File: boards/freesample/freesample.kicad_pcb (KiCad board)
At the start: 8 copper layers, 124 x 190 mm, 576 parts, among them J1 SMA, J10 XILINX_JTAG, J11 SMA, J12 SMA, J13 SMA, J14 SMA, J15 SMA, J16 SMA, J17 SMA, J18 SMA, J19 JUMPER, J2 BARREL, J20 JUMPER, J21 JUMPER, J22 SMA, J23 SMA, J24 SMA, J25 SMA, J26 PMOD_HOST, J3 SMA, J4 SMA, J5 SMA, J6 XILINX_JTAG, J7 CONN_INTEGRALSTICK_FPGA_HOST, J8 CONN_INTEGRALSTICK_MCU_HOST, J9 0826-1G1T-23-F, M1 TRACEPAD, M2 LOGO1, M3 LOGO2, M4 LOGO3, M5 LOGO4, M6 LOGO5, M7 LOGO6, Q1 SSM6N58NU, U1 HMC675LP3E, U10 PI6C59S6005, U11 PI6C59S6005, U12 PI6C59S6005, U13 SIP32408, U14 LMK04806, U15 ASG-D-V-A-125.000MHZ, U16 HMC856, U17 NB6L295, U18 PI6C59S6005, U19 NB7V52MMNG, U2 HMC675LP3E, U20 NB7V52MMNG, U21 NB7V52MMNG, U22 PI6C59S6005, U26 MCP1755ST-5002E/MC, U27 LM27761, U28 ADP1763Z-1.0, U29 ADP1763Z-1.0, U3 PI6C59S6005, U30 OKL-T/3-W12P-C, U31 ADP1741, U32 OKL-T/3-W12P-C, U33 ADP1741, U34 ADP1741, U35 OKL-T/3-W12P-C, U36 OKL-T/3-W12P-C, U37 LM27761, U38 OKL-T/3-W12P-C, U39 LM27761, U4 LTC2664CUH-16#PBF, U40 DS25BR150, U41 DS25BR150, U42 ADP1741, U43 ADP1741, U5 TLK10232, U6 LMK61PD0A2, U7 PI6C59S6005, U8 HMC675LP3E, U9 HMC675LP3E

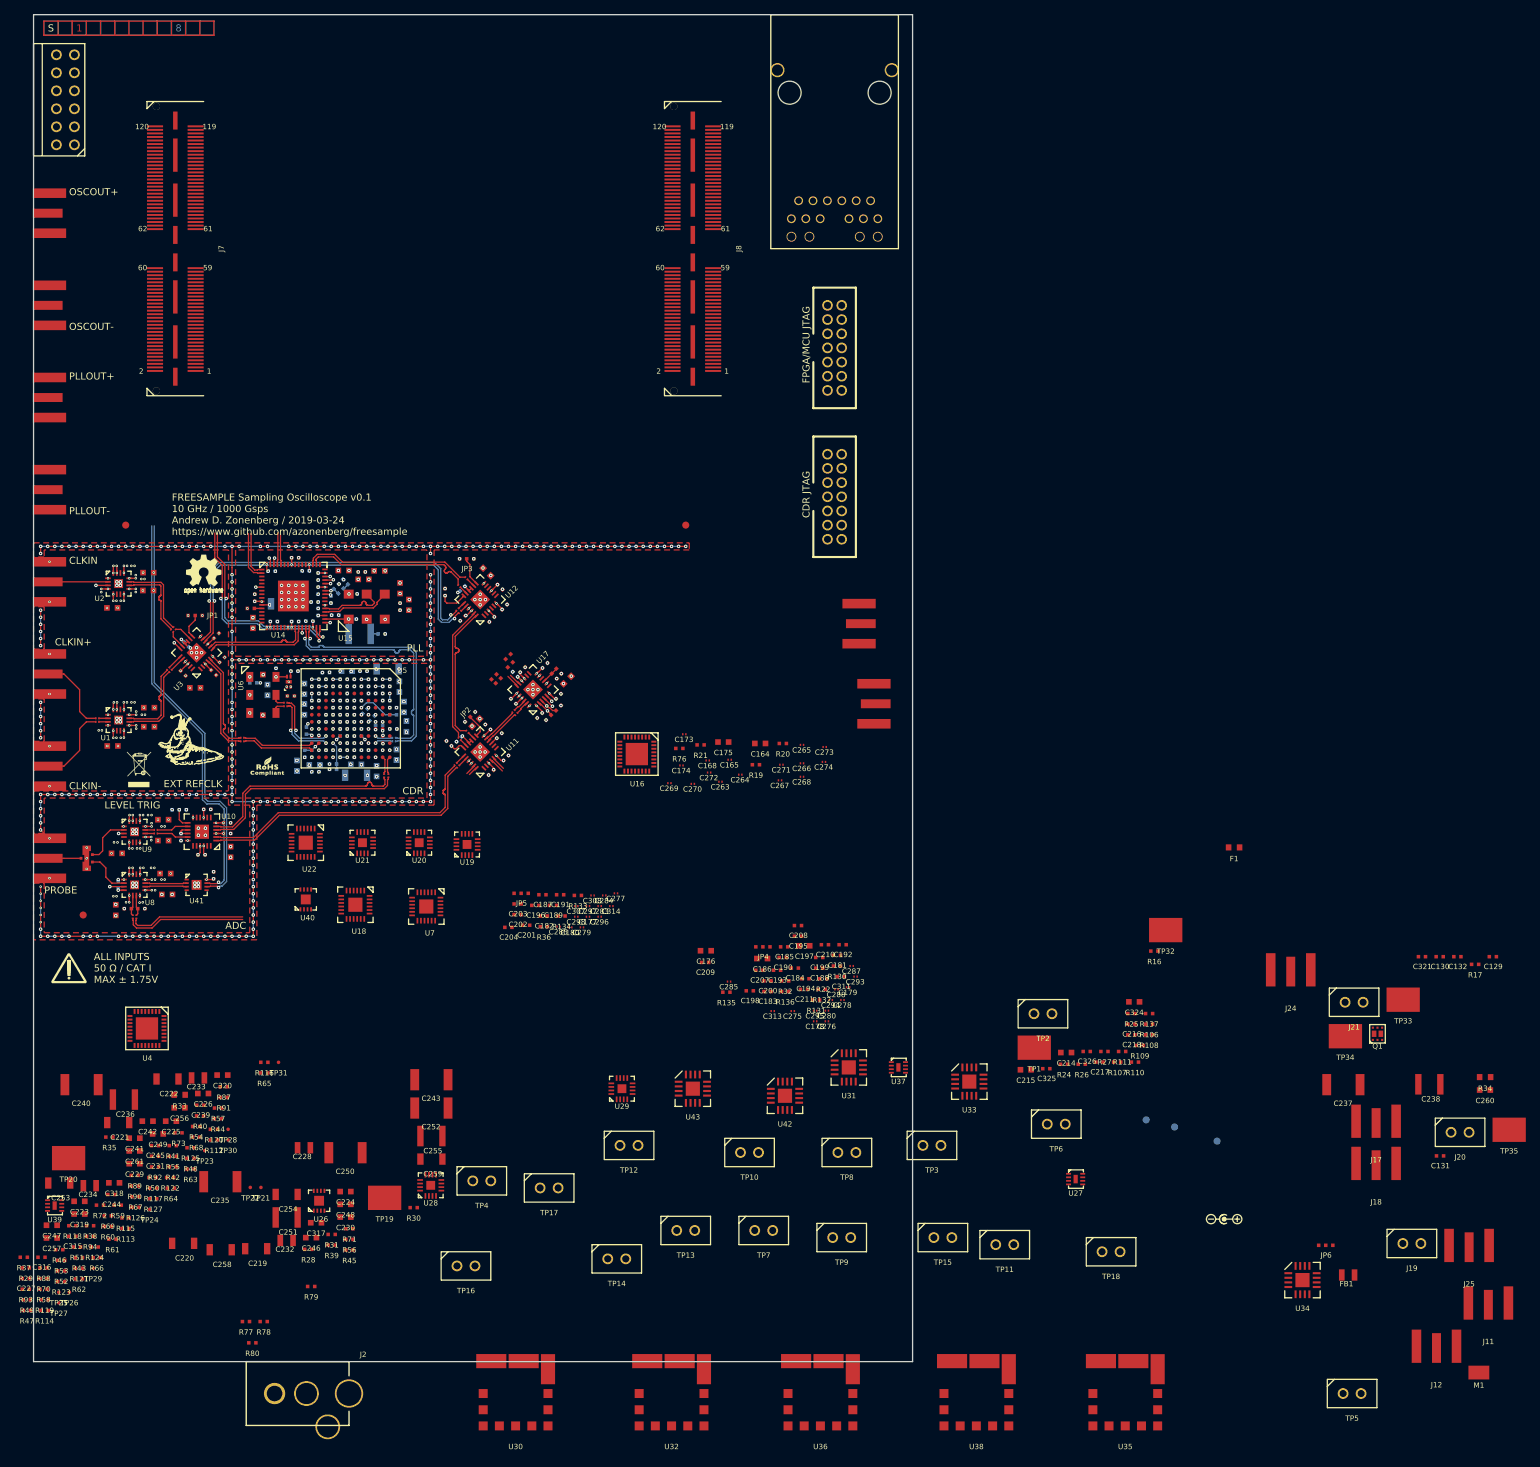
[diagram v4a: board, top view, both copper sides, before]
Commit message: Rearranged a bunch of pending stuff in preparation for further layout. Moved SMAs to approximate final locations
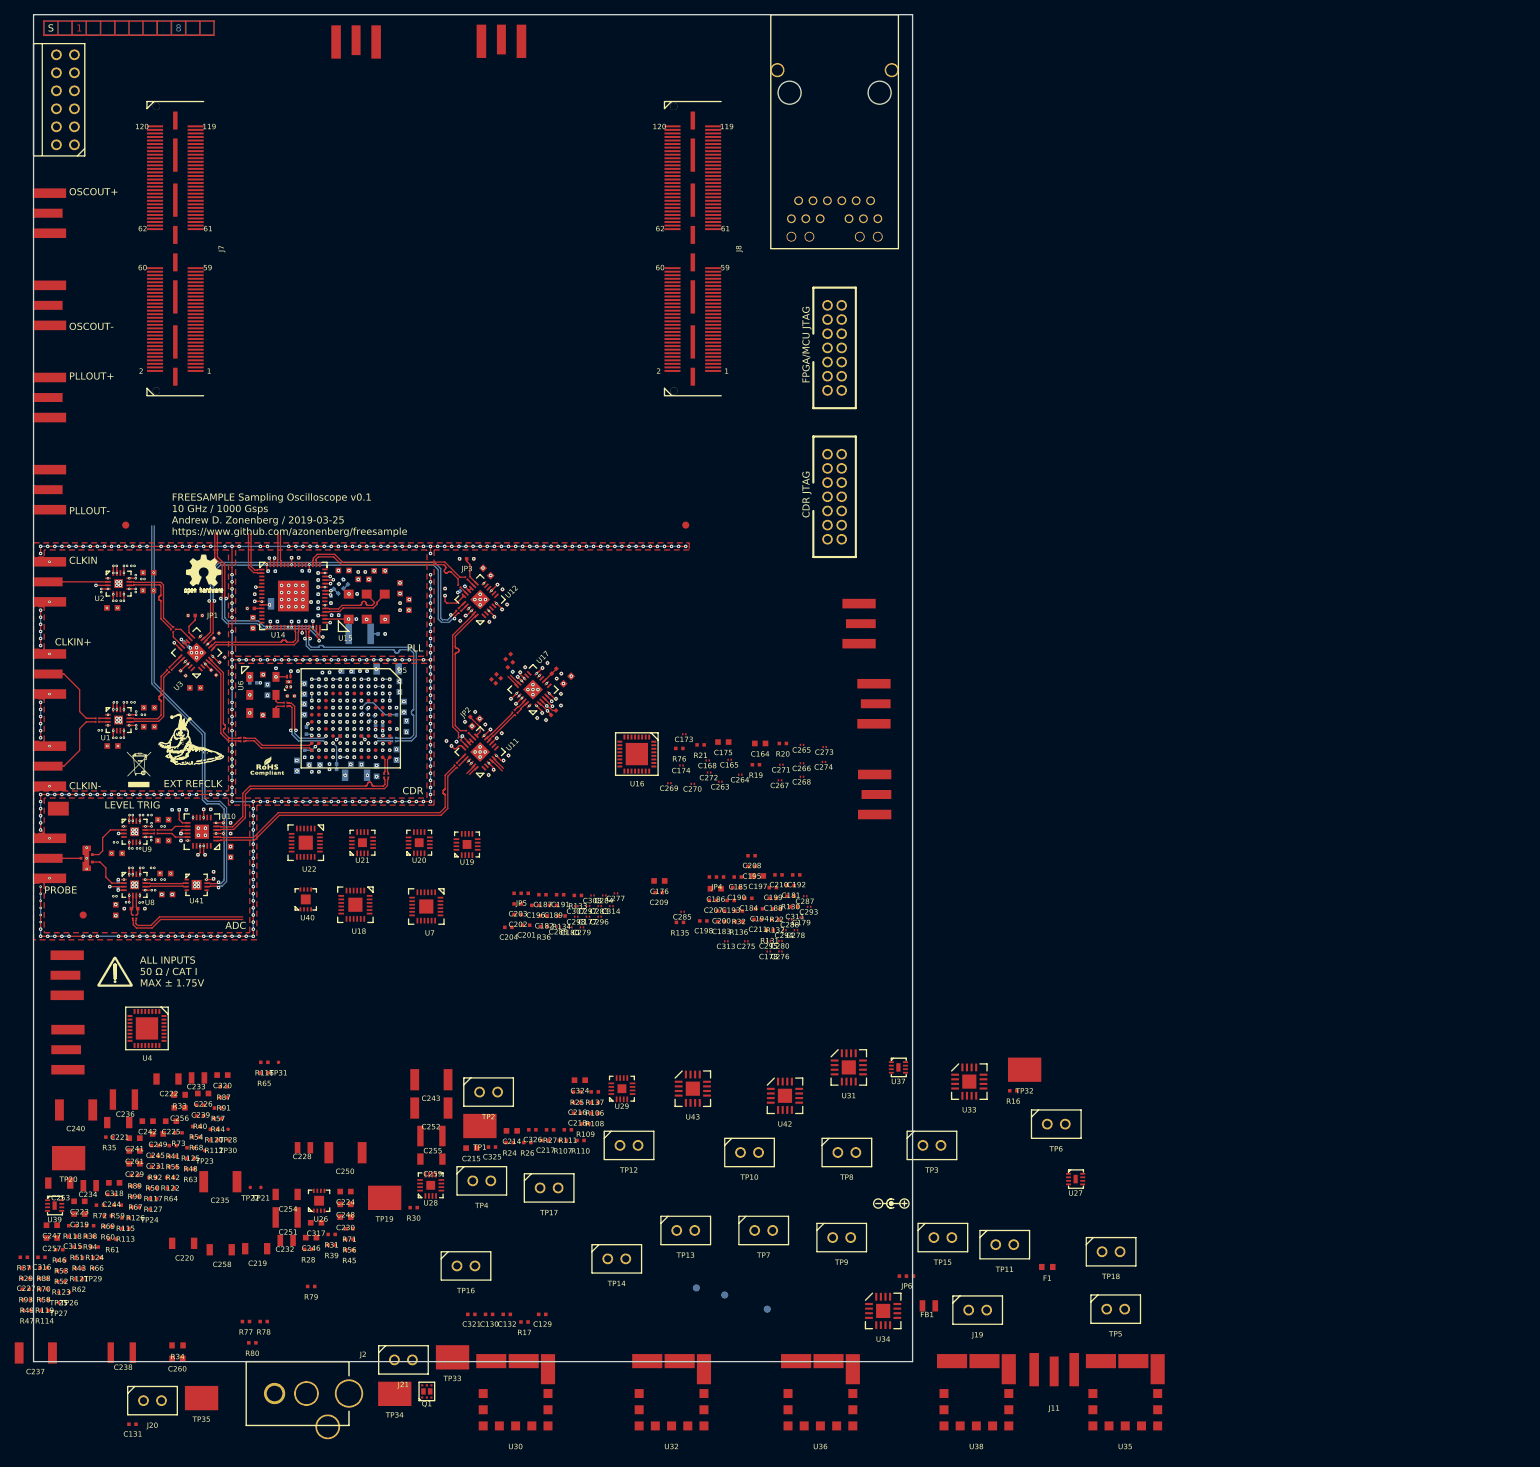
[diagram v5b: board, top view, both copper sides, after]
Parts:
- moved J25 234.7 mm to (61.5, 46.5), turned to 180 degrees
- moved M1 215.6 mm to (19.5, 157.0)
- moved J18 189.2 mm to (18.4, 180.5), turned to 270 degrees
- moved C237 188.3 mm to (16.3, 233.8)
- moved C238 188.3 mm to (28.4, 233.7)
- moved C131 188.3 mm to (30.0, 243.8)
- moved C260 188.3 mm to (36.3, 234.5)
- moved J20 188.3 mm to (32.8, 240.5)
- moved R34 188.3 mm to (36.3, 232.7)
- moved TP35 188.3 mm to (39.7, 240.1)
- moved J17 187.3 mm to (18.5, 191.0), turned to 270 degrees
- moved J24 175.5 mm to (82.0, 46.4), turned to 180 degrees
- moved C129 143.3 mm to (87.8, 228.3)
- moved C130 143.3 mm to (80.3, 228.3)
- moved C132 143.3 mm to (82.8, 228.3)
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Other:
- board text added: "FREESAMPLE Sampling Oscilloscope v0.1 10 GHz / 1000 Gsps Andrew D. Zonenberg / 2019-03-25 https://www.github.com/azonenberg/freesample"
- board text removed: "FREESAMPLE Sampling Oscilloscope v0.1 10 GHz / 1000 Gsps Andrew D. Zonenberg / 2019-03-24 https://www.github.com/azonenberg/freesample"

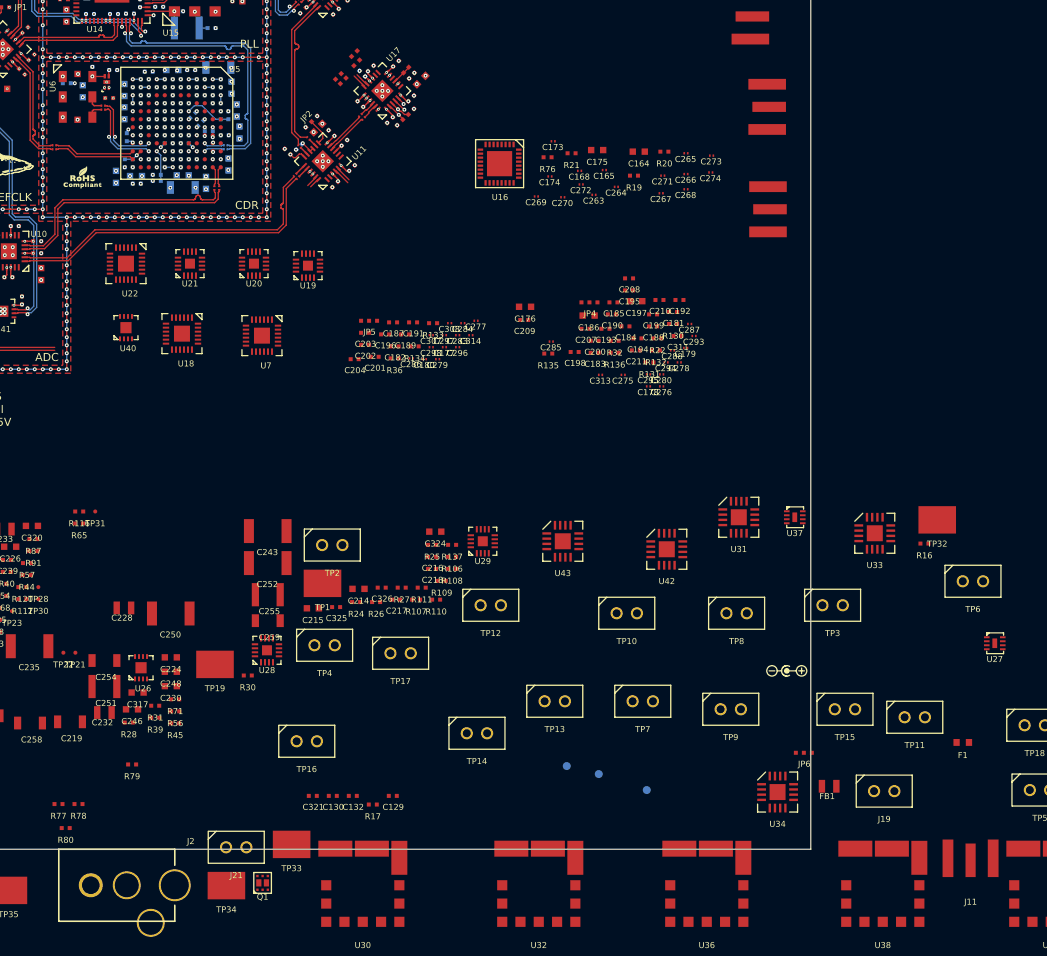
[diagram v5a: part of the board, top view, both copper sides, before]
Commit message: Finished initial layout of delay lines
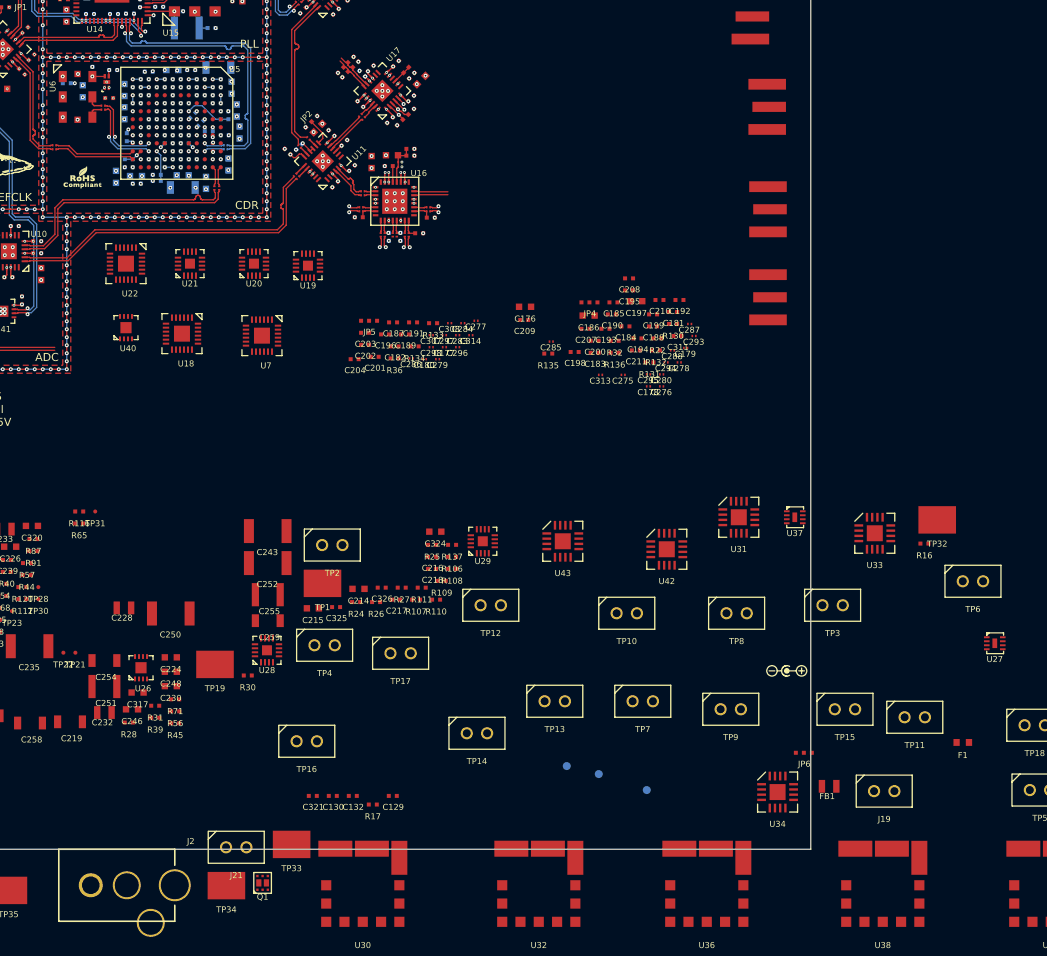
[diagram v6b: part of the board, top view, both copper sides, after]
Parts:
- R77, R78: moved to B.Cu
- moved R80 88.9 mm to (92.5, 156.1), turned to 180 degrees
- moved R77 82.0 mm to (87.2, 158.4), turned to 90 degrees
- moved R78 81.5 mm to (88.7, 158.4), turned to 90 degrees
- moved J11 76.0 mm to (137.0, 166.0), turned to 90 degrees
- moved R79 75.5 mm to (91.0, 158.0), turned to 180 degrees
- moved C273 39.6 mm to (89.2, 158.2), turned to 270 degrees
- moved C274 38.5 mm to (89.8, 158.2), turned to 270 degrees
- moved C265 38.0 mm to (87.8, 158.2), turned to 270 degrees
- moved C266 36.9 mm to (88.2, 158.2), turned to 270 degrees
- moved C271 36.0 mm to (86.2, 158.2), turned to 270 degrees
- moved C164 33.4 mm to (85.1, 149.1), turned to 90 degrees
- moved C268 32.3 mm to (92.2, 155.2)
- moved C264 32.0 mm to (83.8, 155.2), turned to 180 degrees
- moved R20 31.8 mm to (90.0, 148.3), turned to 180 degrees
- moved C267 29.2 mm to (92.2, 154.8)
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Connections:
- U11 pad 23: /Phase control/CLKIN0_N -> (no net)
- U11 pad 24: /Phase control/CLKIN0_P -> (no net)
- U11 pad 4: (no net) -> /Phase control/CLKIN0_N
- U11 pad 5: (no net) -> /Phase control/CLKIN0_P
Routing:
- net /FINE_SEL3_P: track 0.00 -> 54.1 mm, vias 0 -> 1
- net /FINE_SEL3_N: track 0.00 -> 52.9 mm, vias 0 -> 1
- net /FINE_SEL1_N: track 0.00 -> 50.2 mm, vias 0 -> 1
- net /FINE_SEL1_P: track 0.00 -> 49.0 mm, vias 0 -> 1
- net /FINE_SEL0_N: track 0.00 -> 46.1 mm, vias 0 -> 1
- net /FINE_SEL4_N: track 0.00 -> 45.7 mm, vias 0 -> 1
- net /FINE_SEL0_P: track 0.00 -> 45.4 mm, vias 0 -> 1
- net /FINE_SEL4_P: track 0.00 -> 45.0 mm, vias 0 -> 1
- net /3V3_N: track 0.00 -> 44.7 mm, vias 0 -> 19
- net /GND: track 909.2 -> 945.8 mm, vias 560 -> 579
- net /3V3: track 127.9 -> 138.9 mm, vias 45 -> 48
- net /Phase control/DELAY_VR: track 0.00 -> 5.36 mm
- net /Phase control/FINEPHASE_P: track 0.00 -> 4.28 mm
- net /Phase control/FINEPHASE_N: track 0.00 -> 4.28 mm
- net (no net): track 4.13 -> 0.00 mm
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
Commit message: Initial layout work on one-shot. Nowhere near done.
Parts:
- added C212: 0.47 uF, azonenberg_pcb:EIA_0402_CAP_NOSILK, F.Cu at (56.6, 167.4)
- C275, C276, C277, C278, C279, C280, C285, C286, C287, C288, C297, C298, U22: moved to B.Cu
- moved C280 70.5 mm to (51.5, 166.1)
- moved C210 70.3 mm to (50.9, 164.1), turned to 90 degrees
- moved C287 69.4 mm to (55.6, 166.1), turned to 180 degrees
- moved C192 68.0 mm to (56.0, 159.1)
- moved C211 67.6 mm to (50.7, 167.3), turned to 270 degrees
- moved C288 67.5 mm to (55.6, 165.4), turned to 180 degrees
- moved C295 67.2 mm to (53.8, 162.9), turned to 90 degrees
- moved C293 65.5 mm to (60.0, 168.5), turned to 270 degrees
- moved C195 62.1 mm to (55.2, 168.3)
- moved C208 62.1 mm to (55.2, 163.2)
- moved C278 62.0 mm to (62.1, 165.4), turned to 180 degrees
- moved C294 61.7 mm to (60.5, 168.5), turned to 270 degrees
- moved C276 57.8 mm to (64.6, 166.1)
- moved R135 56.7 mm to (52.0, 160.3)
- moved C207 55.6 mm to (56.5, 164.2), turned to 90 degrees
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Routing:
- net /1V8: track 163.1 -> 204.9 mm, vias 35 -> 55
- net /GND: track 945.8 -> 981.5 mm, vias 579 -> 596
- net /One-Shot/SHREG0_P: track 0.00 -> 10.2 mm
- net /One-Shot/SHREG1_N: track 0.00 -> 9.66 mm
- net /One-Shot/SHREG0_N: track 0.00 -> 9.00 mm
- net /One-Shot/SHREG1_P: track 0.00 -> 8.45 mm
- net /ADC/ADC_LE_P: track 16.4 -> 22.6 mm, vias 0 -> 1
- net /ADC/ADC_LE_N: track 17.1 -> 23.2 mm, vias 0 -> 1
- net /Phase control/FINEPHASE_P: track 4.28 -> 1.39 mm
- net /Phase control/FINEPHASE_N: track 4.28 -> 1.39 mm
- net /One-Shot/SHREG2_P: track 0.00 -> 2.50 mm, vias 0 -> 1
- net /One-Shot/SHREG2_N: track 0.00 -> 2.50 mm, vias 0 -> 1
- net /One-Shot/RST1_P: track 0.00 -> 1.83 mm, vias 0 -> 1
- net /One-Shot/RST2_N: track 0.00 -> 1.81 mm, vias 0 -> 1
- net /One-Shot/RST1_N: track 0.00 -> 1.81 mm, vias 0 -> 1
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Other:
- board text added: "FREESAMPLE Sampling Oscilloscope v0.1 10 GHz / 1000 Gsps Andrew D. Zonenberg / 2019-03-31 https://www.github.com/azonenberg/freesample"
- board text removed: "FREESAMPLE Sampling Oscilloscope v0.1 10 GHz / 1000 Gsps Andrew D. Zonenberg / 2019-03-25 https://www.github.com/azonenberg/freesample"
